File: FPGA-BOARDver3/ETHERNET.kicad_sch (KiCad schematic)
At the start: 73 parts, among them J12 HFJ11-1G01ERL, J13 503398-1892, U12 RTL8211F-CG, U13 TXS02612RTWR, U17 NC7WZ07P6X, U18 NL17SZ17XV5T2G, Y1 ABMM-25.000MHZ-B2-T

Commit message: update
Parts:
- D28, D32, D33: footprint LED_SMD:LED_0402_1005Metric -> footprints:LED_0402_1005Metric
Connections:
- net SD_CD: now also R184.1
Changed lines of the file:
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@@
 	)
 	(junction
+		(at 105.41 182.88)
+		(diameter 0)
+		(color 0 0 0 0)
+	)
+	(junction
 		(at 115.57 138.43)
 		(diameter 0)
@@
 	(wire
 		(pts
+			(xy 110.49 173.99) (xy 110.49 182.88)
+		)
+		(stroke
+			(width 0)
+			(type default)
+		)
+	)
+	(wire
+		(pts
 			(xy 60.96 139.7) (xy 60.96 138.43)
 		)
@@
 	(wire
 		(pts
+			(xy 110.49 182.88) (xy 105.41 182.88)
+		)
+		(stroke
+			(width 0)
+			(type default)
+		)
+	)
+	(wire
+		(pts
 			(xy 125.73 107.95) (xy 132.08 107.95)
 		)
@@
 			)
 		)
-		(property "Footprint" "LED_SMD:LED_0402_1005Metric"
+		(property "Footprint" "footprints:LED_0402_1005Metric"
 			(at 191.77 143.51 0)
 			(effects
@@
 			)
 		)
-		(property "Footprint" "LED_SMD:LED_0402_1005Metric"
+		(property "Footprint" "footprints:LED_0402_1005Metric"
 			(at 176.53 143.51 0)
 			(effects
@@
 			)
 		)
-		(property "Footprint" "LED_SMD:LED_0402_1005Metric"
+		(property "Footprint" "footprints:LED_0402_1005Metric"
 			(at 184.15 143.51 0)
 			(effects

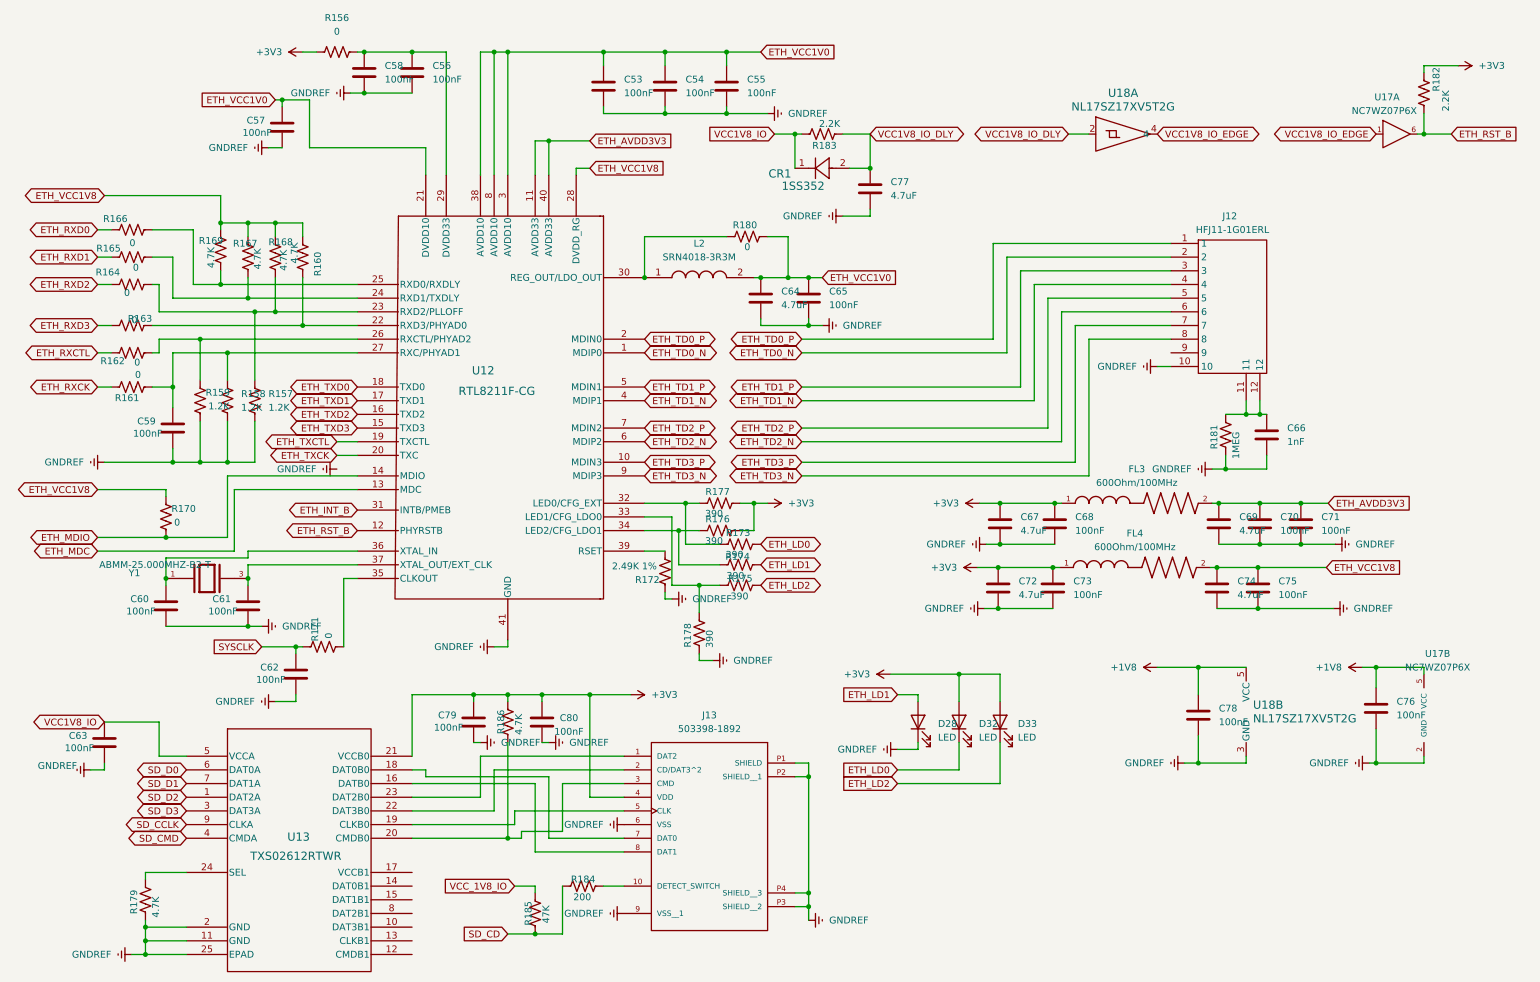
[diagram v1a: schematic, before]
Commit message: added audio out and usb
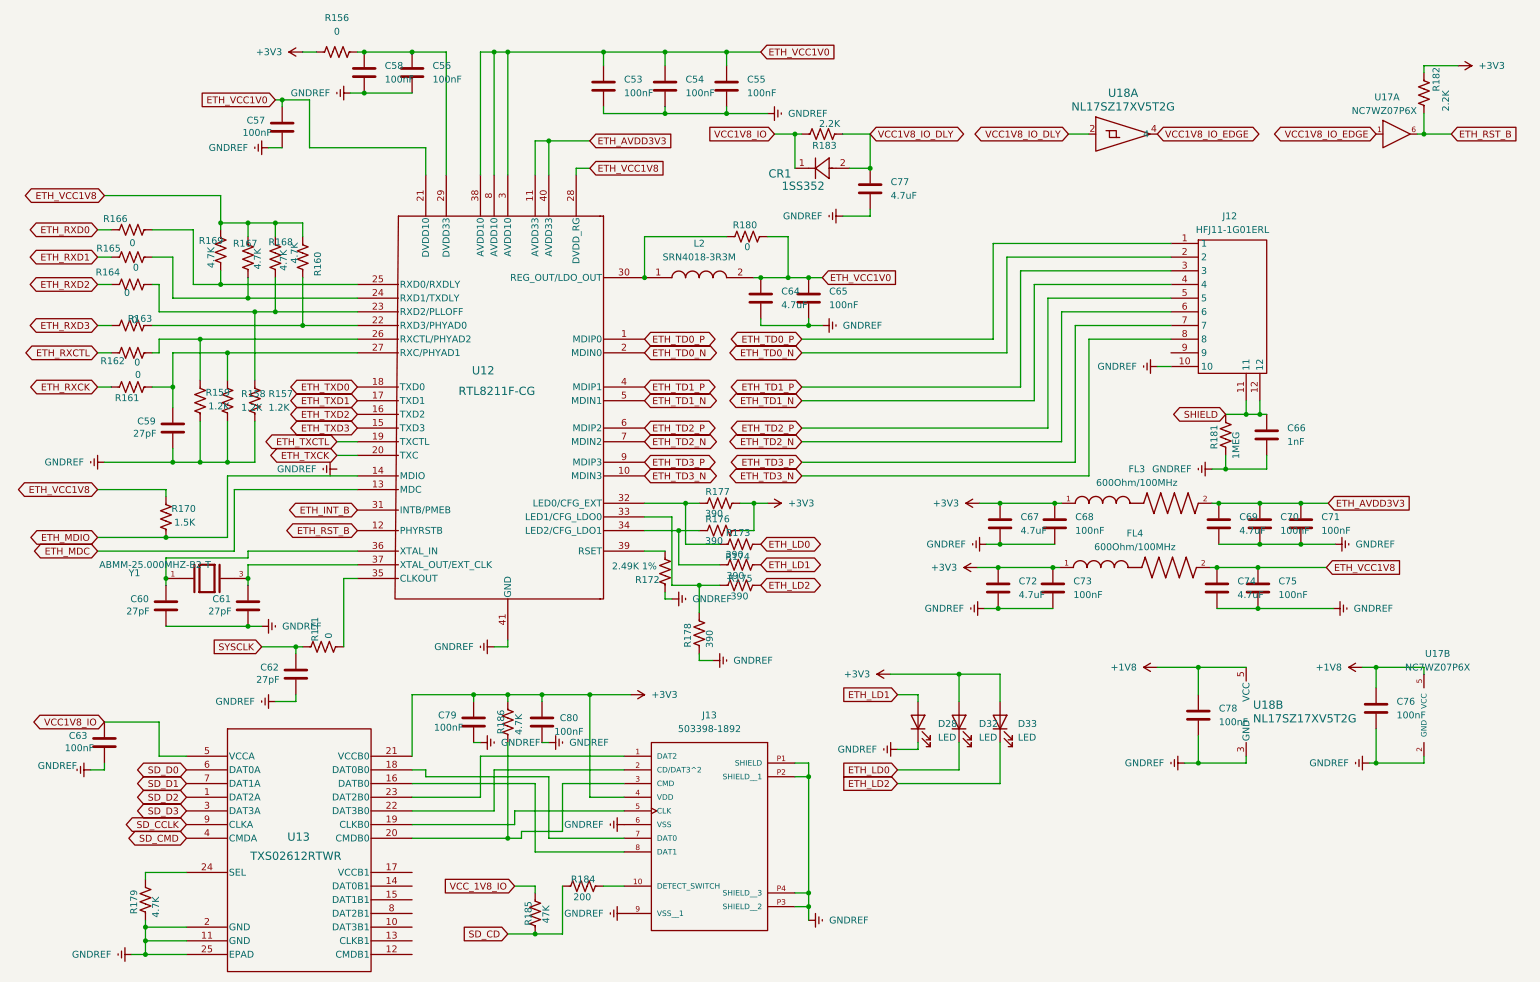
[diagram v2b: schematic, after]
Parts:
- C59, C60, C61, C62: value 100nF -> 27pF
- R170: value 0 -> 1.5K
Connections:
- net ETH_TD0_N: now also U12.2 (MDIN0); no longer U12.1 (MDIP0)
- net ETH_TD0_P: now also U12.1 (MDIP0); no longer U12.2 (MDIN0)
- net ETH_TD1_N: now also U12.5 (MDIN1); no longer U12.4 (MDIP1)
- net ETH_TD1_P: now also U12.4 (MDIP1); no longer U12.5 (MDIN1)
- net ETH_TD2_N: now also U12.7 (MDIN2); no longer U12.6 (MDIP2)
- net ETH_TD2_P: now also U12.6 (MDIP2); no longer U12.7 (MDIN2)
- net ETH_TD3_N: now also U12.10 (MDIN3); no longer U12.9 (MDIP3)
- net ETH_TD3_P: now also U12.9 (MDIP3); no longer U12.10 (MDIN3)
- net SHIELD: now reaches C66.1, J12.11, J12.12, R181.2

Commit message: updated schematic and layout
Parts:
- C53, C54, C55, C56, C57, C63, C65, C68, C70, C71, C73, C75, C76, C78, C79, C80: LCSC PN (none) -> c1525
- C58: value 100nF -> 4.7uF; LCSC PN (none) -> c23733
- C59, C60, C61, C62: LCSC PN (none) -> c472451
- C64, C67, C69, C72, C74, C77: LCSC PN (none) -> c23733
- C66: LCSC PN (none) -> c14442
- CR1: LCSC PN (none) -> C15885
- D28, D32, D33: LCSC PN (none) -> C434449
- FL3, FL4: LCSC PN (none) -> C19330
- J13: LCSC PN (none) -> C428492
- L2: LCSC PN (none) -> C2044390
- R156, R161, R162, R163, R164, R165, R166, R171, R180: LCSC PN (none) -> C106231
- R157, R158, R159: LCSC PN (none) -> C138040
- R160, R167, R168, R169, R179, R186: LCSC PN (none) -> C105871
- R170: LCSC PN (none) -> C114759
- R172: LCSC PN (none) -> C145071
- R173, R174, R175, R176, R177: LCSC PN (none) -> C137997
- R178: value 390 -> 4.7K; LCSC PN (none) -> C105871
- R181: LCSC PN (none) -> C138033
- R182, R183: LCSC PN (none) -> c114762
- R184: LCSC PN (none) -> C114764
- R185: LCSC PN (none) -> C93943
- U12: LCSC PN (none) -> C187932
- U13: LCSC PN (none) -> C140276
- U17: LCSC PN (none) -> C95342
- U18: LCSC PN (none) -> C152502
- Y1: LCSC PN (none) -> C596927
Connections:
- net VCC_1V8_IO is gone; now on net VCC1V8_IO: R185.2
- net +3V3: now also U13.17 (VCCB1); no longer C72.1, C73.1, FL4.1
- net VCC1V8_IO: now also C72.1, C73.1, FL4.1
- net ETH_TXCK renamed ETH_TXCLK
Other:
- moved on the sheet: C72, C73, C74, C75, FL4
